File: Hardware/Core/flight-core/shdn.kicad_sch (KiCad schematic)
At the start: 22 parts, among them J14 Conn_02x02_Remote_ESTOP, J15 Conn_02x07_Counter_Clockwise, J16 Conn_02x02_Remote_ESTOP, J17 TILT, J18 Conn_01x02, J19 Conn_02x02_Remote_ESTOP, J20 Conn_02x02_Remote_ESTOP, J21 Conn_02x02_Remote_ESTOP, J22 Conn_02x02_Remote_ESTOP, J23 Conn_02x02_Remote_ESTOP, J24 Conn_02x02_Remote_ESTOP, J25 Conn_02x02_Remote_ESTOP, J26 Conn_02x02_Remote_ESTOP, Q19 MMBF170, U50 LTV-356T

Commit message: removed extra test points, removed debug2, reannotated schem
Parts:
- renumbered Q19 to Q20, R56 to R57, R57 to R58, R58 to R59, R59 to R60, R60 to R61, R61 to R62
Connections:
- no-connect marks 2 -> 3
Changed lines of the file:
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@@
 		(at 59.69 124.46)
 	)
+	(no_connect
+		(at 58.42 81.28)
+	)
 	(wire
 		(pts
@@
 		(dnp no)
 		(fields_autoplaced yes)
-		(property "Reference" "#PWR0229"
+		(property "Reference" "#PWR0231"
 			(at 138.43 173.99 0)
 			(effects
@@
 			(project "flight-core"
 				(path "/93f46f4b-cdf5-47ec-af03-96378e73b2e1/04eec032-1078-43ee-b9a1-985f3959b29a"
-					(reference "#PWR0229")
+					(reference "#PWR0231")
 					(unit 1)
 				)
@@
 		(dnp no)
 		(fields_autoplaced yes)
-		(property "Reference" "#PWR0230"
+		(property "Reference" "#PWR0232"
 			(at 154.94 173.99 0)
 			(effects
@@
 			(project "flight-core"
 				(path "/93f46f4b-cdf5-47ec-af03-96378e73b2e1/04eec032-1078-43ee-b9a1-985f3959b29a"
-					(reference "#PWR0230")
+					(reference "#PWR0232")
 					(unit 1)
 				)
@@
 		(dnp no)
 		(fields_autoplaced yes)
-		(property "Reference" "R58"
+		(property "Reference" "R59"
 			(at 152.4 161.2899 0)
 			(effects
@@
 			(project "flight-core"
 				(path "/93f46f4b-cdf5-47ec-af03-96378e73b2e1/04eec032-1078-43ee-b9a1-985f3959b29a"
-					(reference "R58")
+					(reference "R59")
 					(unit 1)
 				)
@@
 		(on_board yes)
 		(dnp no)
-		(property "Reference" "#PWR0223"
+		(property "Reference" "#PWR0225"
 			(at 26.67 92.71 0)
 			(effects
@@
 			(project "flight-core"
 				(path "/93f46f4b-cdf5-47ec-af03-96378e73b2e1/04eec032-1078-43ee-b9a1-985f3959b29a"
-					(reference "#PWR0223")
+					(reference "#PWR0225")
 					(unit 1)
 				)
@@
 		(dnp no)
 		(fields_autoplaced yes)
-		(property "Reference" "#PWR0232"
+		(property "Reference" "#PWR0234"
 			(at 264.16 82.55 0)
 			(effects
@@
 			(project "flight-core"
 				(path "/93f46f4b-cdf5-47ec-af03-96378e73b2e1/04eec032-1078-43ee-b9a1-985f3959b29a"
-					(reference "#PWR0232")
+					(reference "#PWR0234")
 					(unit 1)
 				)
@@
 		(dnp no)
 		(fields_autoplaced yes)
-		(property "Reference" "R61"
+		(property "Reference" "R62"
 			(at 271.78 59.6899 0)
 			(effects
@@
 			(project "flight-core"
 				(path "/93f46f4b-cdf5-47ec-af03-96378e73b2e1/04eec032-1078-43ee-b9a1-985f3959b29a"
-					(reference "R61")
+					(reference "R62")
 					(unit 1)
 				)
@@
 		(on_board yes)
 		(dnp no)
-		(property "Reference" "#PWR0222"
+		(property "Reference" "#PWR0224"
 			(at 26.67 85.09 0)
 			(effects
@@
 			(project "flight-core"
 				(path "/93f46f4b-cdf5-47ec-af03-96378e73b2e1/04eec032-1078-43ee-b9a1-985f3959b29a"
-					(reference "#PWR0222")
+					(reference "#PWR0224")
 					(unit 1)
 				)
@@
 		(dnp no)
 		(fields_autoplaced yes)
-		(property "Reference" "#PWR0227"
+		(property "Reference" "#PWR0229"
 			(at 71.12 38.1 0)
 			(effects
@@
 			(project "flight-core"
 				(path "/93f46f4b-cdf5-47ec-af03-96378e73b2e1/04eec032-1078-43ee-b9a1-985f3959b29a"
-					(reference "#PWR0227")
+					(reference "#PWR0229")
 					(unit 1)
 				)
@@
 		(dnp no)
 		(fields_autoplaced yes)
-		(property "Reference" "R60"
+		(property "Reference" "R61"
 			(at 261.62 59.6899 0)
 			(effects
@@
 			(project "flight-core"
 				(path "/93f46f4b-cdf5-47ec-af03-96378e73b2e1/04eec032-1078-43ee-b9a1-985f3959b29a"
-					(reference "R60")
+					(reference "R61")
 					(unit 1)
 				)
@@
 		(on_board yes)
 		(dnp no)
-		(property "Reference" "#PWR0231"
+		(property "Reference" "#PWR0233"
 			(at 161.29 45.72 0)
 			(effects
@@
 			(project "flight-core"
 				(path "/93f46f4b-cdf5-47ec-af03-96378e73b2e1/04eec032-1078-43ee-b9a1-985f3959b29a"
-					(reference "#PWR0231")
+					(reference "#PWR0233")
 					(unit 1)
 				)
@@
 		(on_board yes)
 		(dnp no)
-		(property "Reference" "#PWR0225"
+		(property "Reference" "#PWR0227"
 			(at 43.18 49.53 0)
 			(effects
@@
 			(project "flight-core"
 				(path "/93f46f4b-cdf5-47ec-af03-96378e73b2e1/04eec032-1078-43ee-b9a1-985f3959b29a"
-					(reference "#PWR0225")
+					(reference "#PWR0227")
 					(unit 1)
 				)
@@
 		(on_board yes)
 		(dnp no)
-		(property "Reference" "R59"
+		(property "Reference" "R60"
 			(at 165.735 28.5751 90)
 			(effects
@@
 			(project "flight-core"
 				(path "/93f46f4b-cdf5-47ec-af03-96378e73b2e1/04eec032-1078-43ee-b9a1-985f3959b29a"
-					(reference "R59")
+					(reference "R60")
 					(unit 1)
 				)
@@
 		(dnp no)
 		(fields_autoplaced yes)
-		(property "Reference" "R57"
+		(property "Reference" "R58"
 			(at 135.89 144.7799 0)
 			(effects
@@
 			(project "flight-core"
 				(path "/93f46f4b-cdf5-47ec-af03-96378e73b2e1/04eec032-1078-43ee-b9a1-985f3959b29a"
-					(reference "R57")
+					(reference "R58")
 					(unit 1)
 				)
@@
 		(dnp no)
 		(fields_autoplaced yes)
-		(property "Reference" "#PWR0224"
+		(property "Reference" "#PWR0226"
 			(at 30.48 43.18 0)
 			(effects
@@
 			(project "flight-core"
 				(path "/93f46f4b-cdf5-47ec-af03-96378e73b2e1/04eec032-1078-43ee-b9a1-985f3959b29a"
-					(reference "#PWR0224")
+					(reference "#PWR0226")
 					(unit 1)
 				)
@@
 		(on_board yes)
 		(dnp no)
-		(property "Reference" "Q19"
+		(property "Reference" "Q20"
 			(at 142.24 152.4 0)
 			(effects
@@
 			(project "flight-core"
 				(path "/93f46f4b-cdf5-47ec-af03-96378e73b2e1/04eec032-1078-43ee-b9a1-985f3959b29a"
-					(reference "Q19")
+					(reference "Q20")
 					(unit 1)
 				)
@@
 		(on_board yes)
 		(dnp no)
-		(property "Reference" "R56"
+		(property "Reference" "R57"
 			(at 53.975 98.4251 90)
 			(effects
@@
 			(project "flight-core"
 				(path "/93f46f4b-cdf5-47ec-af03-96378e73b2e1/04eec032-1078-43ee-b9a1-985f3959b29a"
-					(reference "R56")
+					(reference "R57")
 					(unit 1)
 				)
@@
 		(on_board yes)
 		(dnp no)
-		(property "Reference" "#PWR0226"
+		(property "Reference" "#PWR0228"
 			(at 45.72 97.79 0)
 			(effects
@@
 			(project "flight-core"
 				(path "/93f46f4b-cdf5-47ec-af03-96378e73b2e1/04eec032-1078-43ee-b9a1-985f3959b29a"
-					(reference "#PWR0226")
+					(reference "#PWR0228")
 					(unit 1)
 				)
@@
 		(dnp no)
 		(fields_autoplaced yes)
-		(property "Reference" "#PWR0228"
+		(property "Reference" "#PWR0230"
 			(at 138.43 146.05 0)
 			(effects
@@
 			(project ""
 				(path "/93f46f4b-cdf5-47ec-af03-96378e73b2e1/04eec032-1078-43ee-b9a1-985f3959b29a"
-					(reference "#PWR0228")
+					(reference "#PWR0230")
 					(unit 1)
 				)

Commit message: repositioned repeaters to prepare for can routing
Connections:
- net CAN Repeater12/CAN+_OUT: now also J15.13 (Pin_13); no longer J15.14 (Pin_14)
- net CAN Repeater12/CAN-_OUT: now also J15.14 (Pin_14); no longer J15.13 (Pin_13)
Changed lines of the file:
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@@
 	(wire
 		(pts
-			(xy 58.42 76.2) (xy 83.82 76.2)
-		)
-		(stroke
-			(width 0)
-			(type default)
-		)
-	)
-	(wire
-		(pts
 			(xy 238.76 128.27) (xy 236.22 128.27)
 		)
@@
 	(wire
 		(pts
-			(xy 58.42 78.74) (xy 83.82 78.74)
+			(xy 73.66 59.69) (xy 71.12 59.69)
 		)
 		(stroke
@@
 	(wire
 		(pts
-			(xy 73.66 59.69) (xy 71.12 59.69)
+			(xy 238.76 90.17) (xy 236.22 90.17)
 		)
 		(stroke
@@
 	(wire
 		(pts
-			(xy 238.76 90.17) (xy 236.22 90.17)
+			(xy 190.5 77.47) (xy 201.93 77.47)
 		)
 		(stroke
@@
 	(wire
 		(pts
-			(xy 190.5 77.47) (xy 201.93 77.47)
+			(xy 238.76 151.13) (xy 236.22 151.13)
 		)
 		(stroke
@@
 	(wire
 		(pts
-			(xy 238.76 151.13) (xy 236.22 151.13)
+			(xy 238.76 140.97) (xy 236.22 140.97)
 		)
 		(stroke
@@
 	(wire
 		(pts
-			(xy 238.76 140.97) (xy 236.22 140.97)
+			(xy 58.42 76.2) (xy 83.82 76.2)
 		)
 		(stroke
@@
 	(wire
 		(pts
+			(xy 58.42 78.74) (xy 83.82 78.74)
+		)
+		(stroke
+			(width 0)
+			(type default)
+		)
+	)
+	(wire
+		(pts
 			(xy 175.26 62.23) (xy 177.8 62.23)
 		)
@@
 		)
 		(pin "CAN-_OUT" output
-			(at 83.82 78.74 180)
+			(at 83.82 76.2 180)
 			(effects
 				(font
@@
 		)
 		(pin "CAN+_OUT" output
-			(at 83.82 76.2 180)
+			(at 83.82 78.74 180)
 			(effects
 				(font

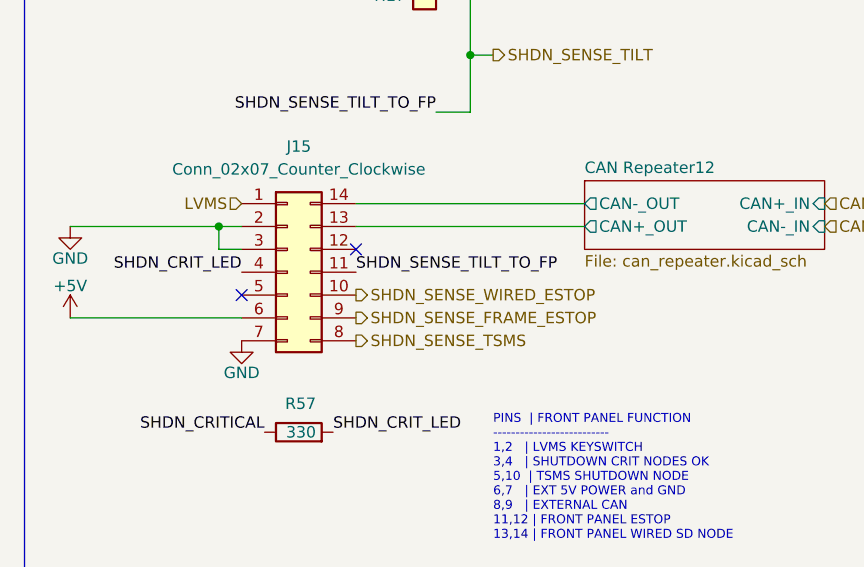
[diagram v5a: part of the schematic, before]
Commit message: modified switchbox connector pinout
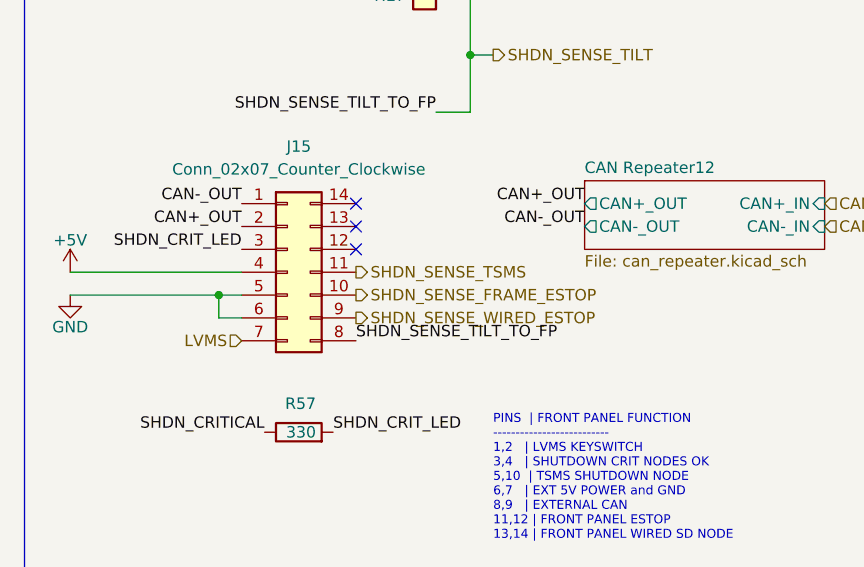
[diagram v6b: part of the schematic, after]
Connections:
- net +5V: now also J15.4 (Pin_4); no longer J15.6 (Pin_6)
- net GND: now also J15.5 (Pin_5), J15.6 (Pin_6); no longer J15.2 (Pin_2), J15.3 (Pin_3), J15.7 (Pin_7)
- net LVMS: now also J15.7 (Pin_7); no longer J15.1 (Pin_1)
- net SHDN_CRIT_LED: now also J15.3 (Pin_3); no longer J15.4 (Pin_4)
- net SHDN_SENSE_FRAME_ESTOP: now also J15.10 (Pin_10); no longer J15.9 (Pin_9)
- net SHDN_SENSE_TILT: now also J15.8 (Pin_8); no longer J15.11 (Pin_11)
- net SHDN_SENSE_TSMS: now also J15.11 (Pin_11); no longer J15.8 (Pin_8)
- net SHDN_SENSE_WIRED_ESTOP: now also J15.9 (Pin_9); no longer J15.10 (Pin_10)
- net CAN Repeater12/CAN+_OUT: no longer names the net of J15.13 (Pin_13)
- net CAN Repeater12/CAN-_OUT: no longer names the net of J15.14 (Pin_14)
- new net CAN+_OUT: J15.2 (Pin_2)
- new net CAN-_OUT: J15.1 (Pin_1)
- no-connect marks 3 -> 4
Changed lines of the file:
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@@
 	)
 	(junction
-		(at 43.18 78.74)
+		(at 43.18 86.36)
 		(diameter 0)
 		(color 0 0 0 0)
@@
 	)
 	(no_connect
-		(at 45.72 86.36)
+		(at 58.42 76.2)
+	)
+	(no_connect
+		(at 58.42 78.74)
 	)
 	(no_connect
@@
 	(wire
 		(pts
-			(xy 43.18 78.74) (xy 45.72 78.74)
+			(xy 43.18 86.36) (xy 45.72 86.36)
 		)
 		(stroke
@@
 	(wire
 		(pts
-			(xy 43.18 81.28) (xy 43.18 78.74)
+			(xy 43.18 88.9) (xy 43.18 86.36)
 		)
 		(stroke
@@
 	(wire
 		(pts
-			(xy 58.42 76.2) (xy 83.82 76.2)
-		)
-		(stroke
-			(width 0)
-			(type default)
-		)
-	)
-	(wire
-		(pts
 			(xy 238.76 100.33) (xy 236.22 100.33)
 		)
@@
 	(wire
 		(pts
-			(xy 45.72 81.28) (xy 43.18 81.28)
+			(xy 45.72 88.9) (xy 43.18 88.9)
 		)
 		(stroke
@@
 	(wire
 		(pts
-			(xy 58.42 78.74) (xy 83.82 78.74)
-		)
-		(stroke
-			(width 0)
-			(type default)
-		)
-	)
-	(wire
-		(pts
 			(xy 175.26 62.23) (xy 177.8 62.23)
 		)
@@
 	(wire
 		(pts
-			(xy 26.67 78.74) (xy 43.18 78.74)
+			(xy 26.67 86.36) (xy 43.18 86.36)
 		)
 		(stroke
@@
 	(wire
 		(pts
-			(xy 26.67 88.9) (xy 45.72 88.9)
+			(xy 26.67 83.82) (xy 45.72 83.82)
 		)
 		(stroke
@@
 	)
 	(label "SHDN_CRIT_LED"
-		(at 45.72 83.82 180)
+		(at 45.72 81.28 180)
 		(effects
 			(font
@@
 	)
 	(label "SHDN_SENSE_TILT_TO_FP"
-		(at 58.42 83.82 0)
+		(at 58.42 91.44 0)
 		(effects
 			(font
@@
 		)
 	)
+	(label "CAN-_OUT"
+		(at 45.72 76.2 180)
+		(effects
+			(font
+				(size 1.27 1.27)
+			)
+			(justify right bottom)
+		)
+	)
+	(label "CAN+_OUT"
+		(at 45.72 78.74 180)
+		(effects
+			(font
+				(size 1.27 1.27)
+			)
+			(justify right bottom)
+		)
+	)
 	(label "CANMSW-"
 		(at 190.5 128.27 0)
@@
 		)
 	)
+	(label "CAN-_OUT"
+		(at 83.82 78.74 180)
+		(effects
+			(font
+				(size 1.27 1.27)
+			)
+			(justify right bottom)
+		)
+	)
 	(label "CANMS+"
 		(at 190.5 113.03 0)
@@
 		)
 	)
+	(label "CAN+_OUT"
+		(at 83.82 76.2 180)
+		(effects
+			(font
+				(size 1.27 1.27)
+			)
+			(justify right bottom)
+		)
+	)
 	(hierarchical_label "SHDN_SENSE_NUC"
 		(shape output)
@@
 	(hierarchical_label "LVMS"
 		(shape input)
-		(at 45.72 76.2 180)
+		(at 45.72 91.44 180)
 		(effects
 			(font
@@
 	(hierarchical_label "SHDN_SENSE_WIRED_ESTOP"
 		(shape output)
-		(at 58.42 86.36 0)
+		(at 58.42 88.9 0)
 		(effects
 			(font
@@
 	(hierarchical_label "SHDN_SENSE_TSMS"
 		(shape output)
-		(at 58.42 91.44 0)
+		(at 58.42 83.82 0)
 		(effects
 			(font
@@
 	(hierarchical_label "SHDN_SENSE_FRAME_ESTOP"
 		(shape output)
-		(at 58.42 88.9 0)
+		(at 58.42 86.36 0)
 		(effects
 			(font
@@
 	(symbol
 		(lib_id "power:+5V")
-		(at 26.67 88.9 0)
+		(at 26.67 83.82 0)
 		(unit 1)
 		(exclude_from_sim no)
@@
 		(dnp no)
 		(property "Reference" "#PWR0225"
-			(at 26.67 92.71 0)
+			(at 26.67 87.63 0)
 			(effects
 				(font
@@
 		)
 		(property "Value" "+5V"
-			(at 26.67 85.344 0)
+			(at 26.67 80.264 0)
 			(effects
 				(font
@@
 		)
 		(property "Footprint" ""
-			(at 26.67 88.9 0)
+			(at 26.67 83.82 0)
 			(effects
 				(font
@@
 		)
 		(property "Datasheet" ""
-			(at 26.67 88.9 0)
+			(at 26.67 83.82 0)
 			(effects
 				(font
@@
 		)
 		(property "Description" "Power symbol creates a global label with name \"+5V\""
-			(at 26.67 88.9 0)
+			(at 26.67 83.82 0)
 			(effects
 				(font
@@
 	(symbol
 		(lib_id "power:GND")
-		(at 26.67 78.74 0)
+		(at 26.67 86.36 0)
 		(unit 1)
 		(exclude_from_sim no)
@@
 		(dnp no)
 		(property "Reference" "#PWR0224"
-			(at 26.67 85.09 0)
+			(at 26.67 92.71 0)
 			(effects
 				(font
@@
 		)
 		(property "Value" "GND"
-			(at 26.67 82.296 0)
+			(at 26.67 89.916 0)
 			(effects
 				(font
@@
 		)
 		(property "Footprint" ""
-			(at 26.67 78.74 0)
+			(at 26.67 86.36 0)
 			(effects
 				(font
@@
 		)
 		(property "Datasheet" ""
-			(at 26.67 78.74 0)
+			(at 26.67 86.36 0)
 			(effects
 				(font
@@
 		)
 		(property "Description" "Power symbol creates a global label with name \"GND\" , ground"
-			(at 26.67 78.74 0)
+			(at 26.67 86.36 0)
 			(effects
 				(font
@@
 	)
 	(symbol
-		(lib_id "power:GND")
-		(at 45.72 91.44 0)
-		(unit 1)
-		(exclude_from_sim no)
-		(in_bom yes)
-		(on_board yes)
-		(dnp no)
-		(property "Reference" "#PWR0228"
-			(at 45.72 97.79 0)
-			(effects
-				(font
-					(size 1.27 1.27)
-				)
-				(hide yes)
-			)
-		)
-		(property "Value" "GND"
-			(at 45.72 94.996 0)
-			(effects
-				(font
-					(size 1.27 1.27)
-				)
-			)
-		)
-		(property "Footprint" ""
-			(at 45.72 91.44 0)
-			(effects
-				(font
-					(size 1.27 1.27)
-				)
-				(hide yes)
-			)
-		)
-		(property "Datasheet" ""
-			(at 45.72 91.44 0)
-			(effects
-				(font
-					(size 1.27 1.27)
-				)
-				(hide yes)
-			)
-		)
-		(property "Description" "Power symbol creates a global label with name \"GND\" , ground"
-			(at 45.72 91.44 0)
-			(effects
-				(font
-					(size 1.27 1.27)
-				)
-				(hide yes)
-			)
-		)
-		(pin "1"
-		)
-		(instances
-			(project "flight-core"
-				(path "/93f46f4b-cdf5-47ec-af03-96378e73b2e1/04eec032-1078-43ee-b9a1-985f3959b29a"
-					(reference "#PWR0228")
-					(unit 1)
-				)
-			)
-		)
-	)
-	(symbol
 		(lib_id "power:+5V")
 		(at 138.43 142.24 0)
@@
 		)
 		(pin "CAN-_OUT" output
-			(at 83.82 76.2 180)
+			(at 83.82 78.74 180)
 			(effects
 				(font
@@
 		)
 		(pin "CAN+_OUT" output
-			(at 83.82 78.74 180)
+			(at 83.82 76.2 180)
 			(effects
 				(font

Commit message: Major reroute & semi-final update
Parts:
- removed J17: TILT, footprints:MicroFit_V_2, symbol Connector_Generic:Conn_01x02
- removed J18: Conn_01x02, footprints:MicroFit_V_2, symbol Connector_Generic:Conn_01x02
- added J3201: Conn_02x02_Remote_ESTOP, Connector_Molex:Molex_Micro-Fit_3.0_43045-0412_2x02_P3.00mm_Vertical, symbol Connector_Generic:Conn_02x02_Counter_Clockwise
- added JP3301, JP3302: SolderJumper_2_Bridged, Jumper:SolderJumper-2_P1.3mm_Bridged2Bar_RoundedPad1.0x1.5mm, symbol Jumper:SolderJumper_2_Bridged
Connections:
- net +5V: now also J15.6 (Pin_6), J3201.1 (Pin_1); no longer J15.4 (Pin_4)
- net CAN+: now also JP3302.2 (B); no longer R61.1
- net CAN+_OUT: now also J15.14 (Pin_14); no longer J15.2 (Pin_2)
- net CAN-: now also JP3301.1 (A); no longer R62.1
- net CAN-_OUT: now also J15.13 (Pin_13); no longer J15.1 (Pin_1)
- net GND: now also J15.2 (Pin_2), J15.3 (Pin_3), J15.7 (Pin_7), J3201.2 (Pin_2); no longer J15.5 (Pin_5), J15.6 (Pin_6)
- net LVMS: now also J15.1 (Pin_1); no longer J15.7 (Pin_7)
- net SHDN_CRIT_LED: now also J15.4 (Pin_4); no longer J15.3 (Pin_3)
- net SHDN_SENSE_FRAME_ESTOP: now also J15.9 (Pin_9); no longer J15.10 (Pin_10)
- net SHDN_SENSE_REMOTE_ESTOP: now also J3201.4 (Pin_4)
- net SHDN_SENSE_TILT: now also J15.11 (Pin_11), J3201.3 (Pin_3); no longer J15.8 (Pin_8)
- net SHDN_SENSE_TSMS: now also J15.8 (Pin_8); no longer J15.11 (Pin_11)
- net SHDN_SENSE_WIRED_ESTOP: now also J15.10 (Pin_10); no longer J15.9 (Pin_9)
- new net: JP3301.2 (B), R62.1
- new net: JP3302.1 (A), R61.1
- no-connect marks 4 -> 3
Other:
- moved on the sheet: J14

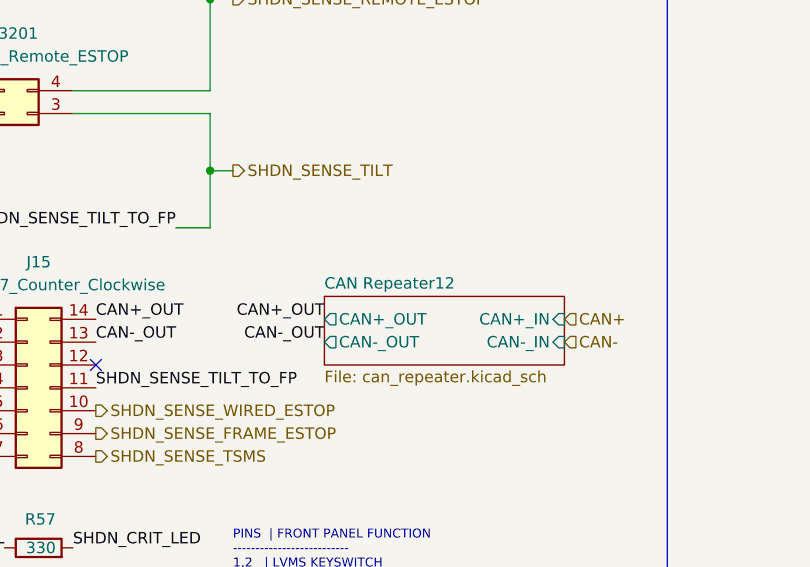
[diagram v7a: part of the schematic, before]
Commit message: moving silkscreen, renaming can repeater sheet name
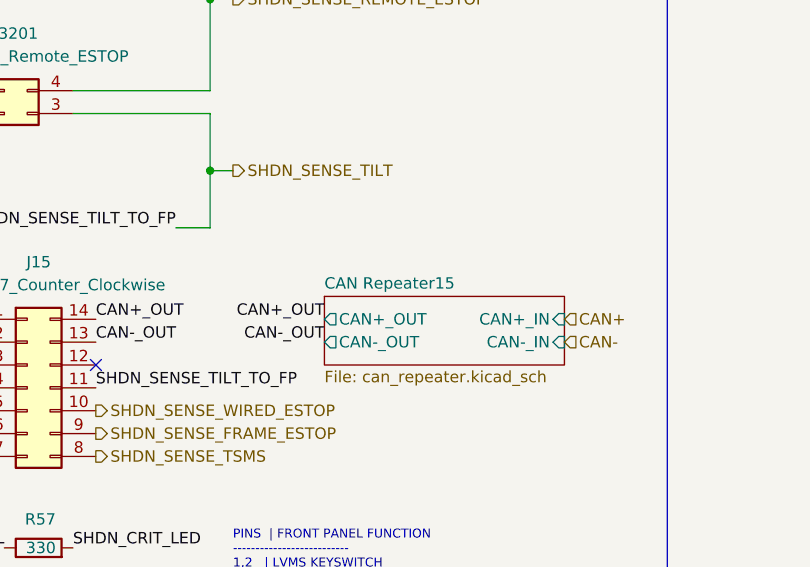
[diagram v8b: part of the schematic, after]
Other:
- sheet CAN Repeater12 renamed CAN Repeater15
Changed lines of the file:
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@@
 			(color 0 0 0 0.0000)
 		)
-		(property "Sheetname" "CAN Repeater12"
+		(property "Sheetname" "CAN Repeater15"
 			(at 83.82 72.9484 0)
 			(effects
